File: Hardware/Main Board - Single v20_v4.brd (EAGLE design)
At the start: 86.4 x 73.7 mm, 117 parts, among them J1 MICROMOD-2222-C, J10 MICRO-SD-PUSH-PUSH-EXT-PIN, J2 Vertical Qwiic Connector, J4 QWIIC_RIGHT_ANGLE, J5 CORTEX_JTAG_DEBUG_MINIMUM_PTH, J6 MICROMOD_FUNCTION_MAIN, Q1 3.1A/30V/105mΩ, Q2 20V/4.2A/52mΩ/1.4W, U1 STG3856QTR, U2 MCP73831, U3 ESD Diode, U4 AP7347DQ-33W5-7K-3.3V, U5 AP7361C-33

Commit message: Rolls version to v20
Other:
- board text added: "v20"
- board text removed: "v13"
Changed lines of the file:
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@@
 <wire x1="0" y1="0" x2="0" y2="73.66" width="0.2032" layer="20"/>
 <wire x1="86.36" y1="0" x2="86.36" y2="73.66" width="0.2032" layer="20"/>
-<text x="76.1492" y="71.7296" size="1.27" layer="16" font="vector" ratio="15" rot="MR180" align="center">v13</text>
+<text x="76.1492" y="71.7296" size="1.27" layer="16" font="vector" ratio="15" rot="MR180" align="center">v20</text>
 <text x="43.18" y="-25.654" size="1.778" layer="51" font="vector">Elias Santistevan</text>
 <text x="50.673" y="-14.859" size="1.778" layer="47" font="vector" ratio="15" rot="R180">Units in Inches</text>
@@
 <wire x1="78.994" y1="10.9564" x2="78.9596" y2="10.922" width="0.2032" layer="16"/>
 <wire x1="78.9596" y1="10.922" x2="69.7738" y2="10.922" width="0.2032" layer="16"/>
-<wire x1="56.476" y1="50.038" x2="56.576" y2="50.138" width="0.5588" layer="1"/>
 <wire x1="56.476" y1="50.038" x2="57.404" y2="50.038" width="0.5588" layer="1"/>
 <wire x1="57.404" y1="50.038" x2="58.039" y2="50.673" width="0.5588" layer="1"/>
@@
 <contactref element="U3" pad="5"/>
 <wire x1="78.3336" y1="63.4492" x2="78.3336" y2="64.2112" width="0.2032" layer="1"/>
-<wire x1="76.0003" y1="63.246" x2="74.93" y2="63.246" width="0.2032" layer="1"/>
-<via x="74.93" y="63.246" extent="1-16" drill="0.3048"/>
-<wire x1="74.93" y1="63.246" x2="79.3242" y2="63.246" width="0.2032" layer="16"/>
+<wire x1="76.0003" y1="63.246" x2="74.9046" y2="63.246" width="0.2032" layer="1"/>
+<via x="74.9046" y="63.246" extent="1-16" drill="0.3048"/>
+<wire x1="74.9046" y1="63.246" x2="79.3242" y2="63.246" width="0.2032" layer="16"/>
 </signal>
 <signal name="N$6">

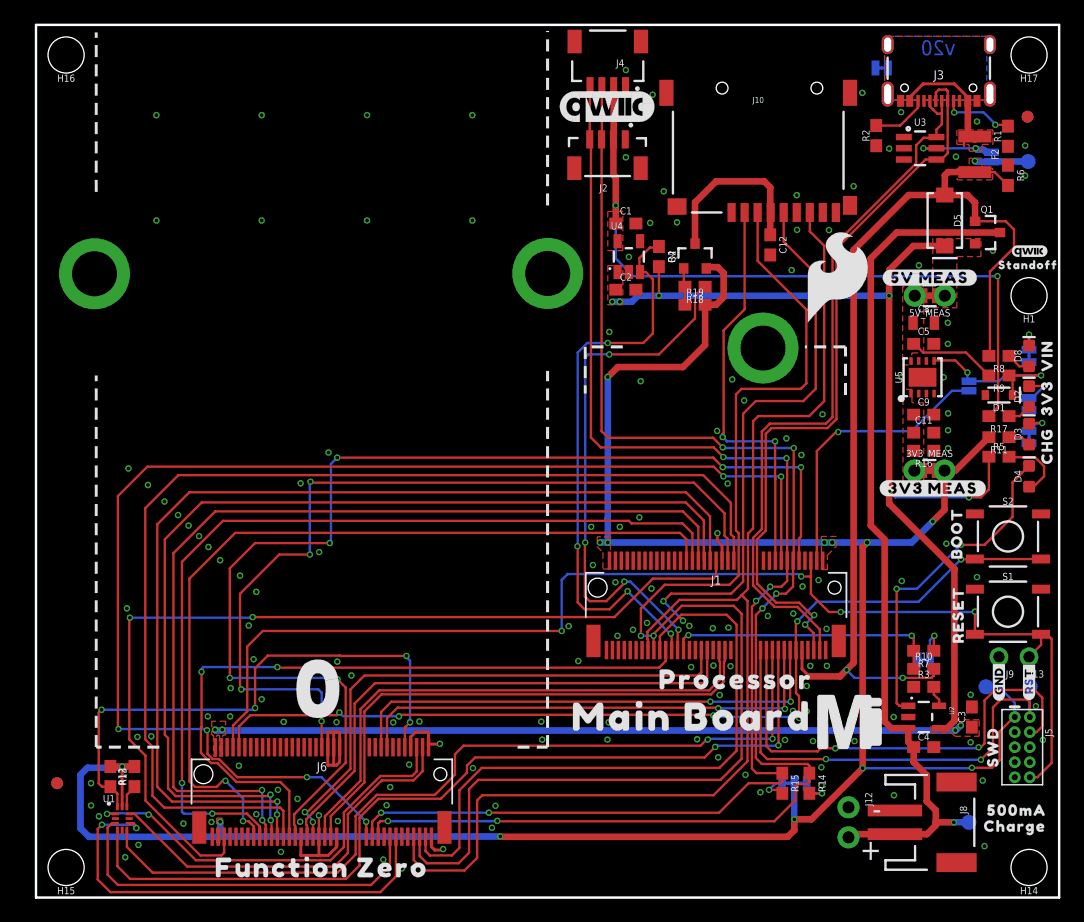
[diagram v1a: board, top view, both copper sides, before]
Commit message: * Adds 4-pin header for other DFU lines
* Updates silk
* Uses VIN as power supply to battery charger
* Fixes PCH Mosfet
* Fixes polygons where applicable
* Adds SparkFun logo to topside.
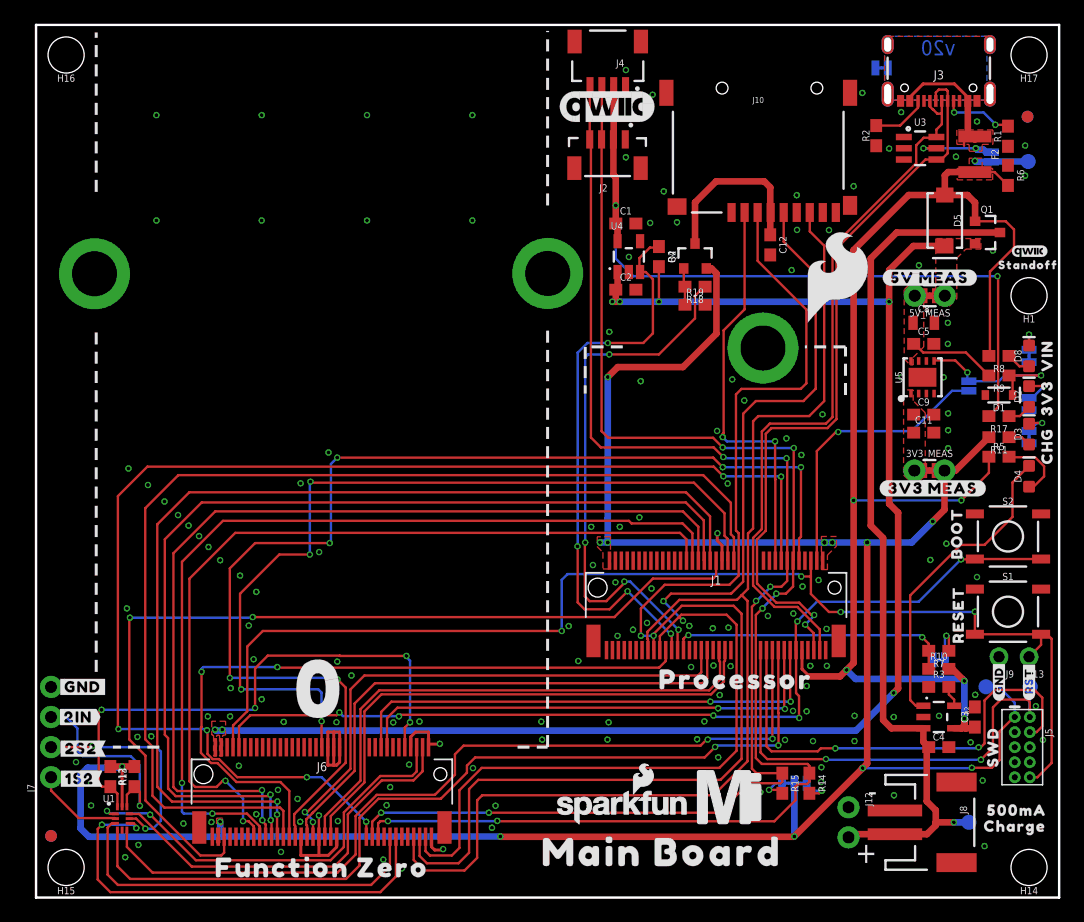
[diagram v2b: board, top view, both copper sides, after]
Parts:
- removed R16: 2.2M, SparkFun-Resistors:0603
- added J7: (no value), SparkFun-Connectors:1X04_NO_SILK
- added U$1: (no value), top:#1S2#3
- added U$12: (no value), top:#2IN#0
- added U$16, U$29: (no value), top:#GND#3
- added U$19: (no value), bot:#1S2#3
- added U$2: (no value), top:#2S2#3
- added U$20: (no value), bot:#2IN#0
- added U$28: (no value), bot:#2S2#3
- added U$32: (no value), top:SWD6522
- added U$34: (no value), SparkFun-Aesthetics:SFE_LOGO_NAME_FLAME_.1
- moved U$14 12.0 mm to (58.5, 8.51)
- moved U$21 11.7 mm to (52.8, 3.84)
- moved FD1 4.47 mm to (1.27, 5.21)
- moved FD2 4.47 mm to (1.27, 5.21)
- moved C4 1.27 mm to (76.2, 12.7)
- moved DIVIDER 1.27 mm to (76.2, 20.1)
- moved R10 1.27 mm to (76.2, 19.3)
- moved R3 1.27 mm to (76.2, 17.8)
- moved R7 1.27 mm to (76.2, 20.8)
- moved U2 1.27 mm to (76.2, 15.2)
- moved C3 0.25 mm to (79.2, 15.2)
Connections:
- net I2C_SDA1-PROCESSOR/!SD_DISABLE! renamed I2C_SDA1-PROCESSOR/!SD_ENABLE!
- removed net !DFU-FC1!: R12.1, U1.P10
- removed net N$1: 3V3_MEAS.1, 3V3_MEAS.3, C11.1, C9.1, R16.2, U5.1
- new net 1S2_MULTIPLEXER: J7.1, U1.P2
- new net 2IN_MULTIPLEXER: J7.3, R12.1, U1.P10
- new net 2S2_MULTIPLEXER: J7.2, U1.P8
- new net 3V3_MEAS: 3V3_MEAS.1, 3V3_MEAS.3, C11.1, C9.1, U5.1
- net 3.3V: no longer R19.2
- net GND: now also J7.4, R19.2; no longer R16.1
- net VCC: no longer C3.1, R5.1, U2.4
- net VIN: now also C3.1, R5.1, U2.4
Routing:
- net VIN: track 91.1 -> 115.3 mm, vias 3 -> 6
- net 2S2_MULTIPLEXER: track 0.00 -> 18.7 mm, vias 0 -> 2
- net VCC: track 148.3 -> 129.9 mm, vias 10 -> 7
- net 2IN_MULTIPLEXER: track 0.00 -> 17.5 mm, vias 0 -> 1
- net 1S2_MULTIPLEXER: track 0.00 -> 7.54 mm
- net !DFU-FC1!: track 1.96 -> 0.00 mm
- net 3.3V_QWIIC: track 61.2 -> 62.8 mm
- net N$8: track 27.9 -> 26.4 mm, vias 2 -> 0
- net VIN/3: track 23.2 -> 24.2 mm
- net V_BATT: track 73.4 -> 74.2 mm
- net 3.3V: track 198.2 -> 197.7 mm
- net GND: vias 154 -> 155
- added copper zone on layer 1, net 3V3_MEAS
- removed copper zone on layer 1, net 3.3V_QWIIC
- removed copper zone on layer 1, net N$1

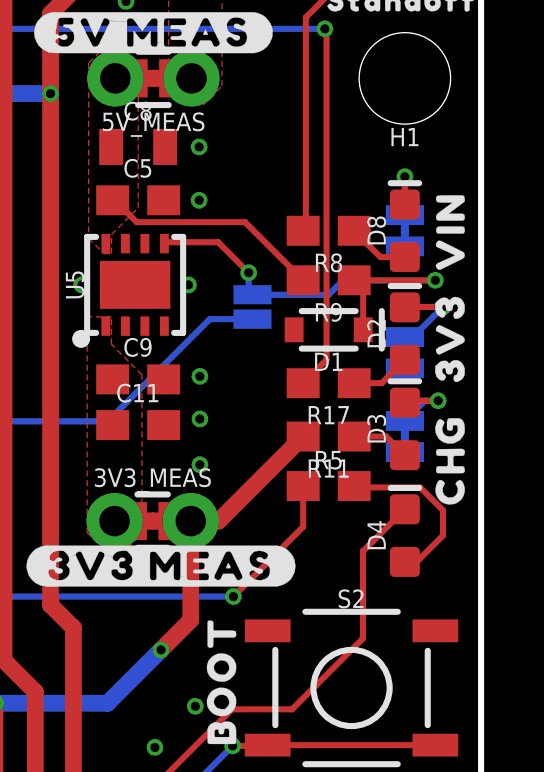
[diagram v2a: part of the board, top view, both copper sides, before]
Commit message: Adds qwiic LED silk
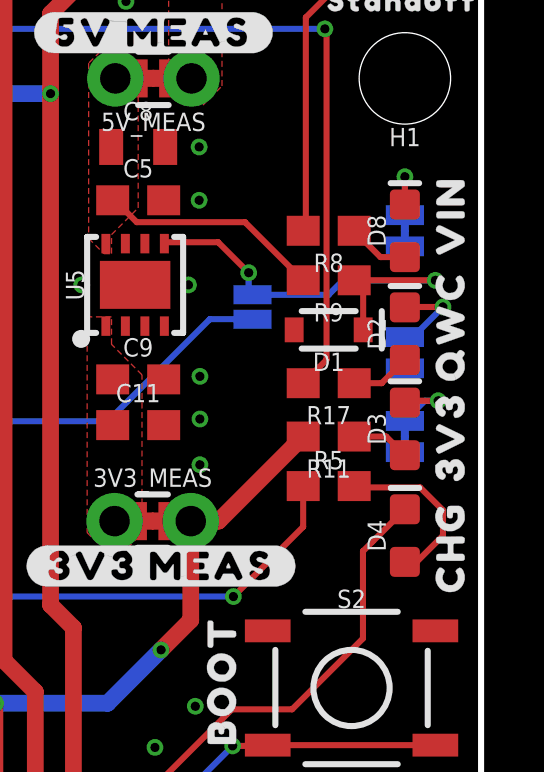
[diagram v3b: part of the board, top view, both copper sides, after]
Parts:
- added U$35: (no value), top:QWC4
- moved U$4 3.30 mm to (85.3, 38.9)
- moved U$6 2.92 mm to (85.3, 35.2)
- moved U$5 0.51 mm to (85.3, 46.2)
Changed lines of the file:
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@@
 <attribute name="PROD_ID" value="HW-14899" x="43.1924" y="52.6796" size="1.778" layer="27" rot="R90" display="off"/>
 </element>
-<element name="U$4" library="top" package="3V332533" value="" x="85.344" y="42.164" smashed="yes" rot="R90"/>
-<element name="U$5" library="top" package="VIN32532" value="" x="85.344" y="45.72" smashed="yes" rot="R90"/>
-<element name="U$6" library="top" package="CHG32531" value="" x="85.344" y="38.1" smashed="yes" rot="R90"/>
+<element name="U$4" library="top" package="3V332533" value="" x="85.344" y="38.862" smashed="yes" rot="R90"/>
+<element name="U$5" library="top" package="VIN32532" value="" x="85.344" y="46.228" smashed="yes" rot="R90"/>
+<element name="U$6" library="top" package="CHG32531" value="" x="85.344" y="35.179" smashed="yes" rot="R90"/>
 <element name="U$8" library="top" package="BOOT32541" value="" x="77.724" y="30.734" smashed="yes" rot="R90"/>
 <element name="U$9" library="top" package="RESET32540" value="" x="77.851" y="23.876" smashed="yes" rot="R90"/>
@@
 <element name="U$32" library="top" package="SWD6522" value="" x="80.645" y="12.7" smashed="yes" rot="MR90"/>
 <element name="U$34" library="SparkFun-Aesthetics" package="SFE_LOGO_NAME_FLAME_.1" value="" x="49.53" y="7.62" smashed="yes"/>
+<element name="U$35" library="top" package="QWC4" value="" x="85.344" y="42.545" smashed="yes" rot="R90"/>
 </elements>
 <signals>

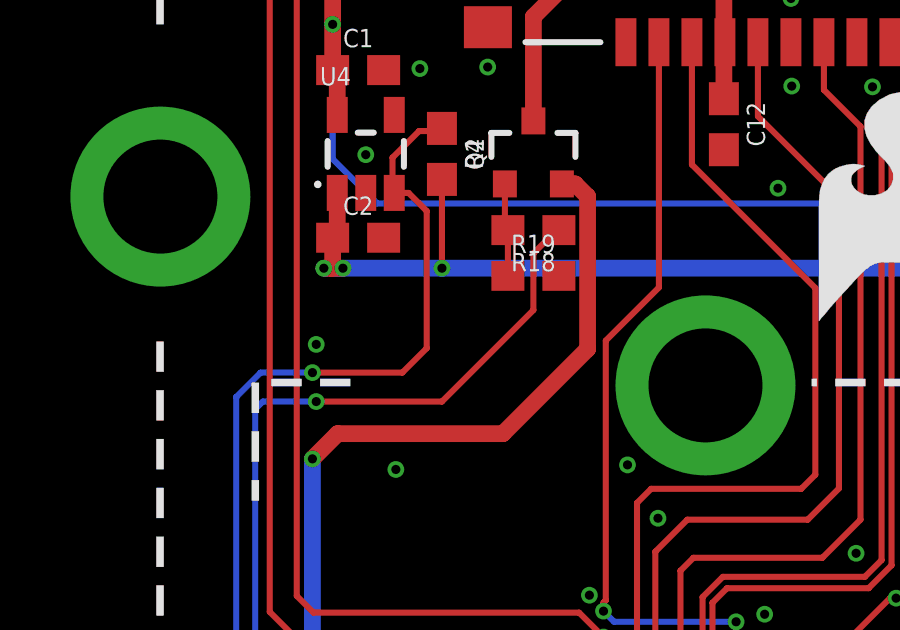
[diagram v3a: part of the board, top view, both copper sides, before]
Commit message: Fixes airwire
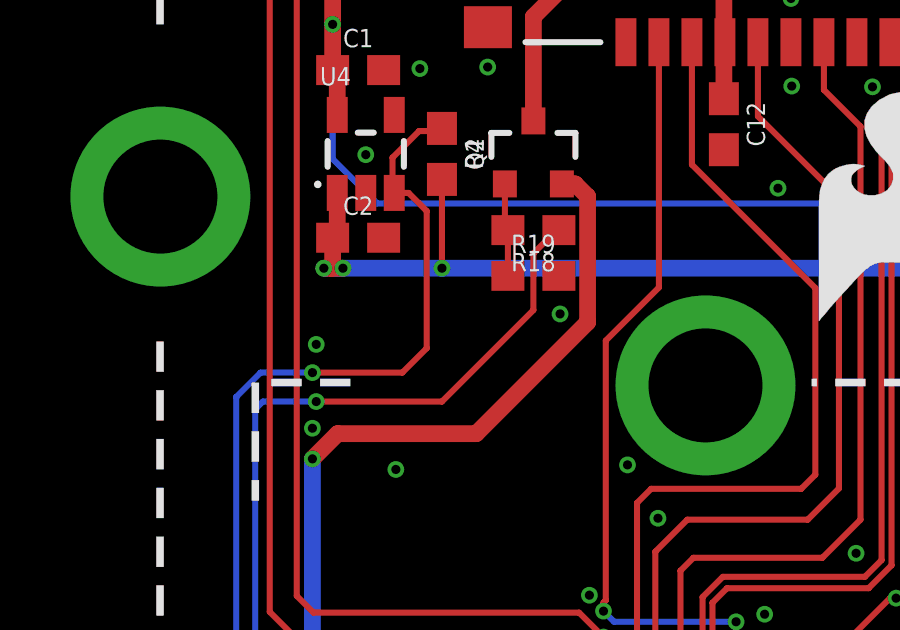
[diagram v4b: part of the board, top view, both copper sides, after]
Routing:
- net 3.3V: track 197.7 -> 197.1 mm
- net GND: vias 155 -> 157
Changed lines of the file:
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@@
 <via x="3.3782" y="11.43" extent="1-16" drill="0.3048"/>
 <via x="76.2254" y="15.3416" extent="1-16" drill="0.3048"/>
-<wire x1="56.476" y1="50.038" x2="50.634" y2="51.308" width="0" layer="19" extent="1-1"/>
+<via x="56.515" y="48.768" extent="1-16" drill="0.3048"/>
+<via x="48.26" y="44.958" extent="1-16" drill="0.3048"/>
 </signal>
 <signal name="V_BATT" class="1">
@@
 <contactref element="I2C_PU" pad="2"/>
 <wire x1="48.2604" y1="43.9372" x2="49.1006" y2="44.7774" width="0.5588" layer="1"/>
-<wire x1="49.1006" y1="44.7774" x2="54.61" y2="44.7774" width="0.5588" layer="1"/>
+<wire x1="49.1006" y1="44.7774" x2="53.721" y2="44.7774" width="0.5588" layer="1"/>
 <wire x1="64.008" y1="9.652" x2="64.008" y2="5.1562" width="0.5588" layer="16"/>
 <via x="64.008" y="5.1562" extent="1-16" drill="0.3048"/>
@@
 <wire x1="57.4324" y1="52.6875375" x2="57.0179375" y2="53.102" width="0.5588" layer="1"/>
 <wire x1="56.576" y1="53.102" x2="57.0179375" y2="53.102" width="0.5588" layer="1"/>
-<wire x1="57.4324" y1="47.5998" x2="57.4324" y2="52.6875375" width="0.5588" layer="1"/>
-<wire x1="54.61" y1="44.7774" x2="57.4324" y2="47.5998" width="0.5588" layer="1"/>
-<wire x1="11.43" y1="5.1308" x2="11.43" y2="5.1308" width="0.5588" layer="16"/>
+<wire x1="57.4324" y1="48.4888" x2="57.4324" y2="52.6875375" width="0.5588" layer="1"/>
+<wire x1="53.721" y1="44.7774" x2="57.4324" y2="48.4888" width="0.5588" layer="1"/>
 </signal>
 <signal name="3.3V_EN">
